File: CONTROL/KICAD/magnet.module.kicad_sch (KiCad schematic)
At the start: 0 parts

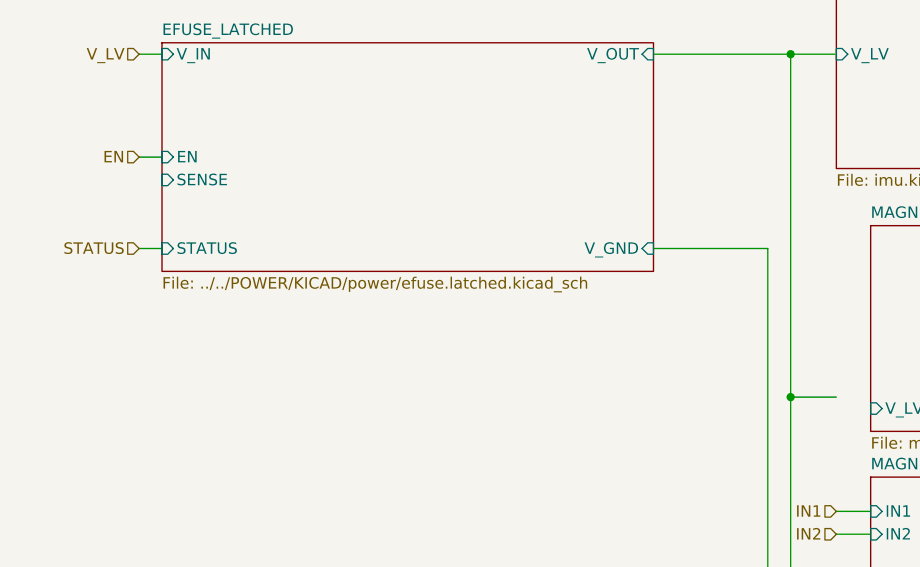
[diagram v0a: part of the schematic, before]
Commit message: Edited Schematics
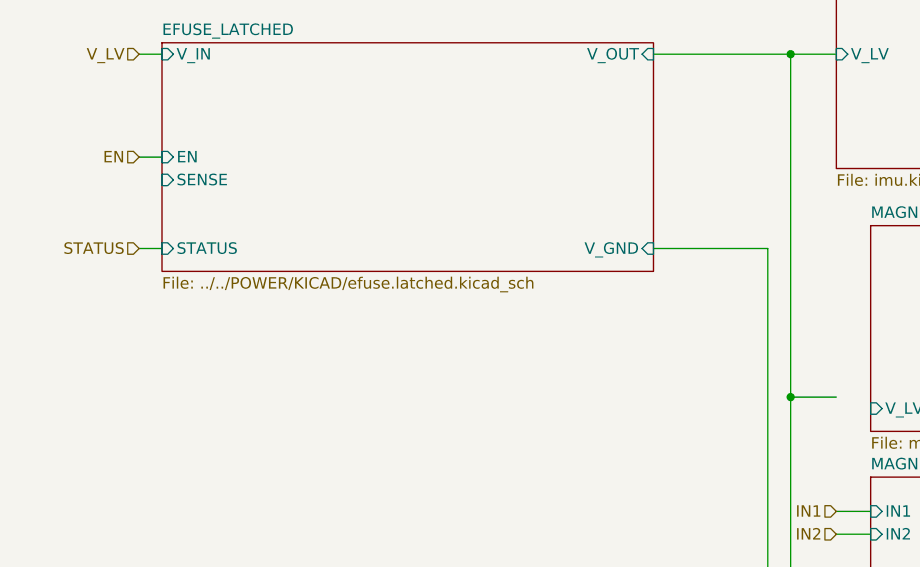
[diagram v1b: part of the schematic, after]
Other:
- sheet EFUSE_LATCHED: file ../../POWER/KICAD/power/efuse.latched.kicad_sch -> ../../POWER/KICAD/efuse.latched.kicad_sch
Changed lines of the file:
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@@
 			)
 		)
-		(property "Sheetfile" "../../POWER/KICAD/power/efuse.latched.kicad_sch"
+		(property "Sheetfile" "../../POWER/KICAD/efuse.latched.kicad_sch"
 			(at 78.74 89.4846 0)
 			(effects

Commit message: Updated Control PCB / Schematics
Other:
- removed sheet IMU
- removed sheet MAGNETOMETER
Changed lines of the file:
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@@
-		)
-	)
-	(sheet
-		(at 157.48 83.82)
-		(size 35.56 22.86)
-		(fields_autoplaced yes)
-		(stroke
-			(width 0.1524)
-			(type solid)
-		)
-		(fill
-			(color 0 0 0 0.0000)
-		)
-		(property "Sheetname" "MAGNETOMETER"
-			(at 157.48 83.1084 0)
-			(effects
-				(font
-					(size 1.27 1.27)
-				)
-				(justify left bottom)
-			)
-		)
-		(property "Sheetfile" "magnetometer.kicad_sch"
-			(at 157.48 107.2646 0)
-			(effects
-				(font
-					(size 1.27 1.27)
-				)
-				(justify left top)
-			)
-		)
-		(pin "V_GND" input
-			(at 193.04 104.14 0)
-			(effects
-				(font
-					(size 1.27 1.27)
-				)
-				(justify right)
-			)
-		)
-		(pin "V_LV" input
-			(at 157.48 104.14 180)
-			(effects
-				(font
-					(size 1.27 1.27)
-				)
-				(justify left)
-			)
-		)
-		(instances
-			(project "control"
-				(path "/c4b3c8f9-82bd-4648-8d22-870bf16aa829/8812c96e-ca04-41e1-abbd-8267da6f4a17"
-					(page "6")
-				)
-			)
-		)
-	)
-	(sheet
-		(at 153.67 54.61)
-		(size 25.4 22.86)
-		(fields_autoplaced yes)
-		(stroke
-			(width 0.1524)
-			(type solid)
-		)
-		(fill
-			(color 0 0 0 0.0000)
-		)
-		(property "Sheetname" "IMU"
-			(at 153.67 53.8984 0)
-			(effects
-				(font
-					(size 1.27 1.27)
-				)
-				(justify left bottom)
-			)
-		)
-		(property "Sheetfile" "imu.kicad_sch"
-			(at 153.67 78.0546 0)
-			(effects
-				(font
-					(size 1.27 1.27)
-				)
-				(justify left top)
-			)
-		)
-		(pin "V_GND" input
-			(at 179.07 74.93 0)
-			(effects
-				(font
-					(size 1.27 1.27)
-				)
-				(justify right)
-			)
-		)
-		(pin "INT2" input
-			(at 179.07 67.31 0)
-			(effects
-				(font
-					(size 1.27 1.27)
-				)
-				(justify right)
-			)
-		)
-		(pin "INT1" input
-			(at 179.07 64.77 0)
-			(effects
-				(font
-					(size 1.27 1.27)
-				)
-				(justify right)
-			)
-		)
-		(pin "V_LV" input
-			(at 153.67 64.77 180)
-			(effects
-				(font
-					(size 1.27 1.27)
-				)
-				(justify left)
-			)
-		)
-		(instances
-			(project "control"
-				(path "/c4b3c8f9-82bd-4648-8d22-870bf16aa829/8812c96e-ca04-41e1-abbd-8267da6f4a17"
-					(page "5")
-				)
-			)
 		)
 	)
